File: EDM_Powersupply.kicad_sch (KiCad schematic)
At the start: 23 parts, among them J1 Screw_Terminal_01x02, Q1 IPW65R037C6, U1 L7805, U2 STGAP2SM, U3 RP2040, U4 MGJ2D051505SC, U5 LMV331

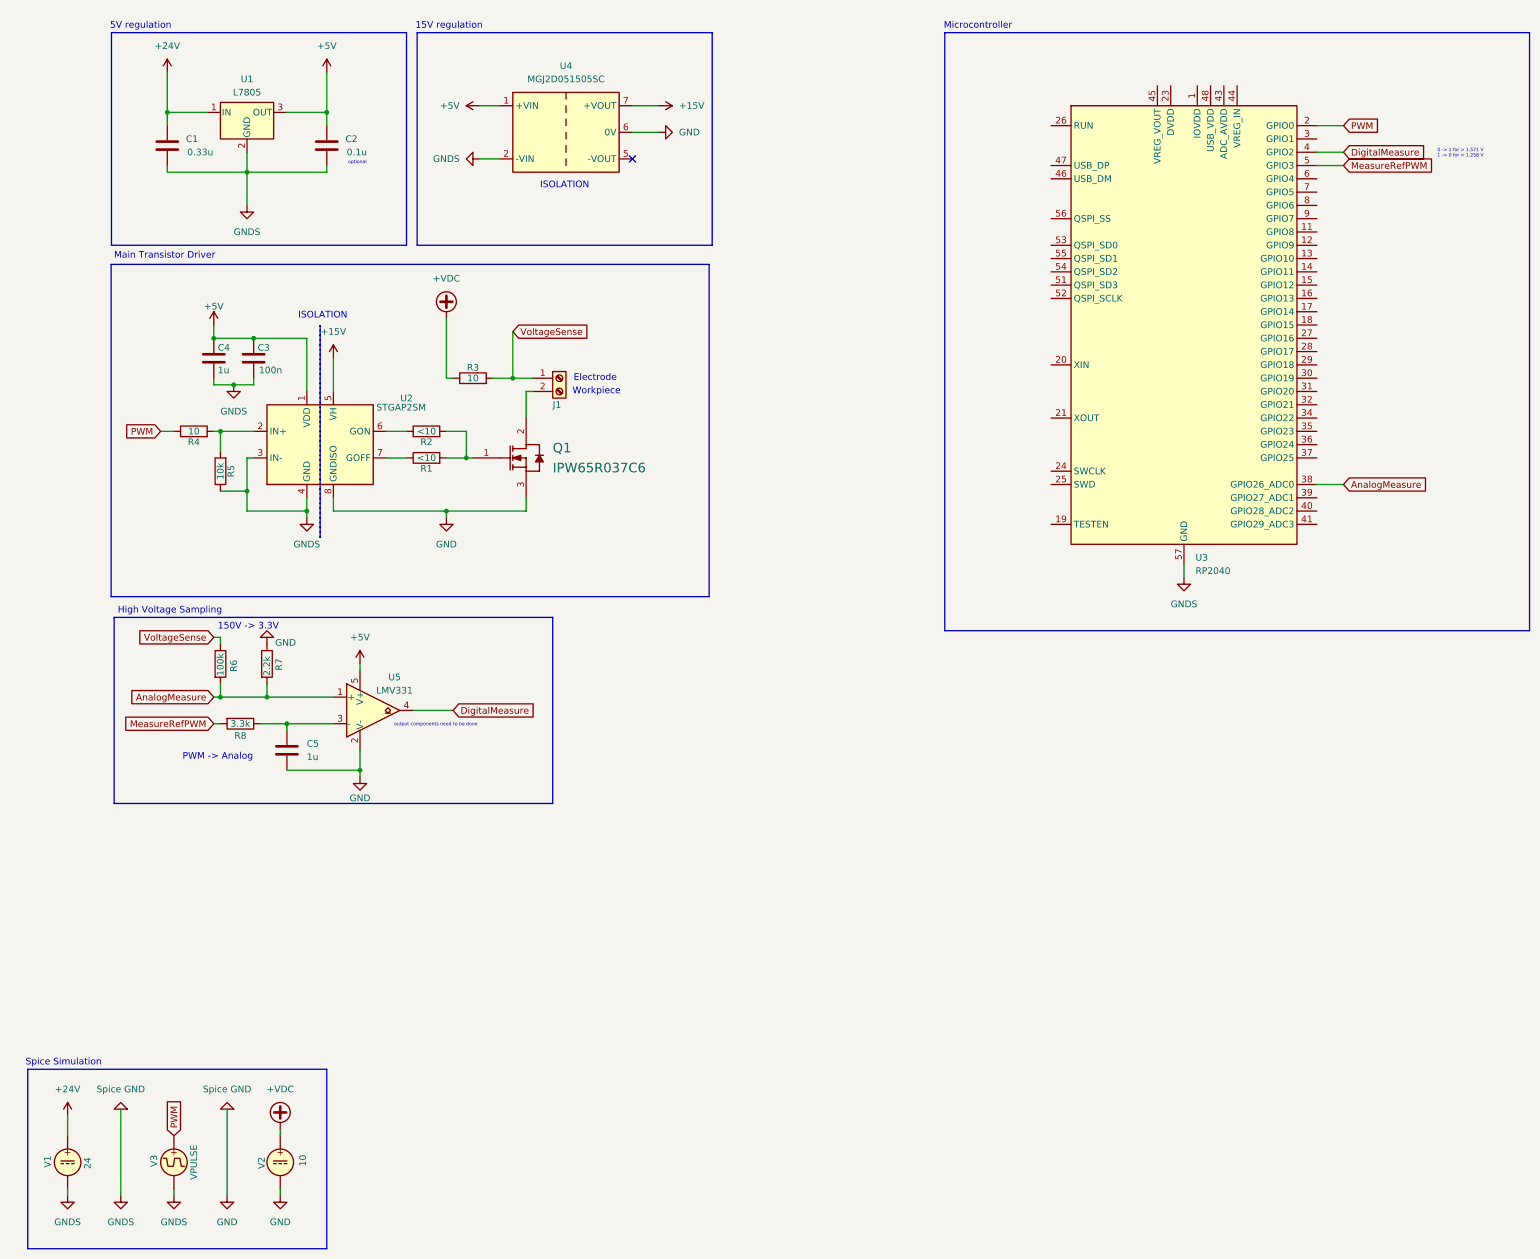
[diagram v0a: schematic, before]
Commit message: Full Reordering and added test pads
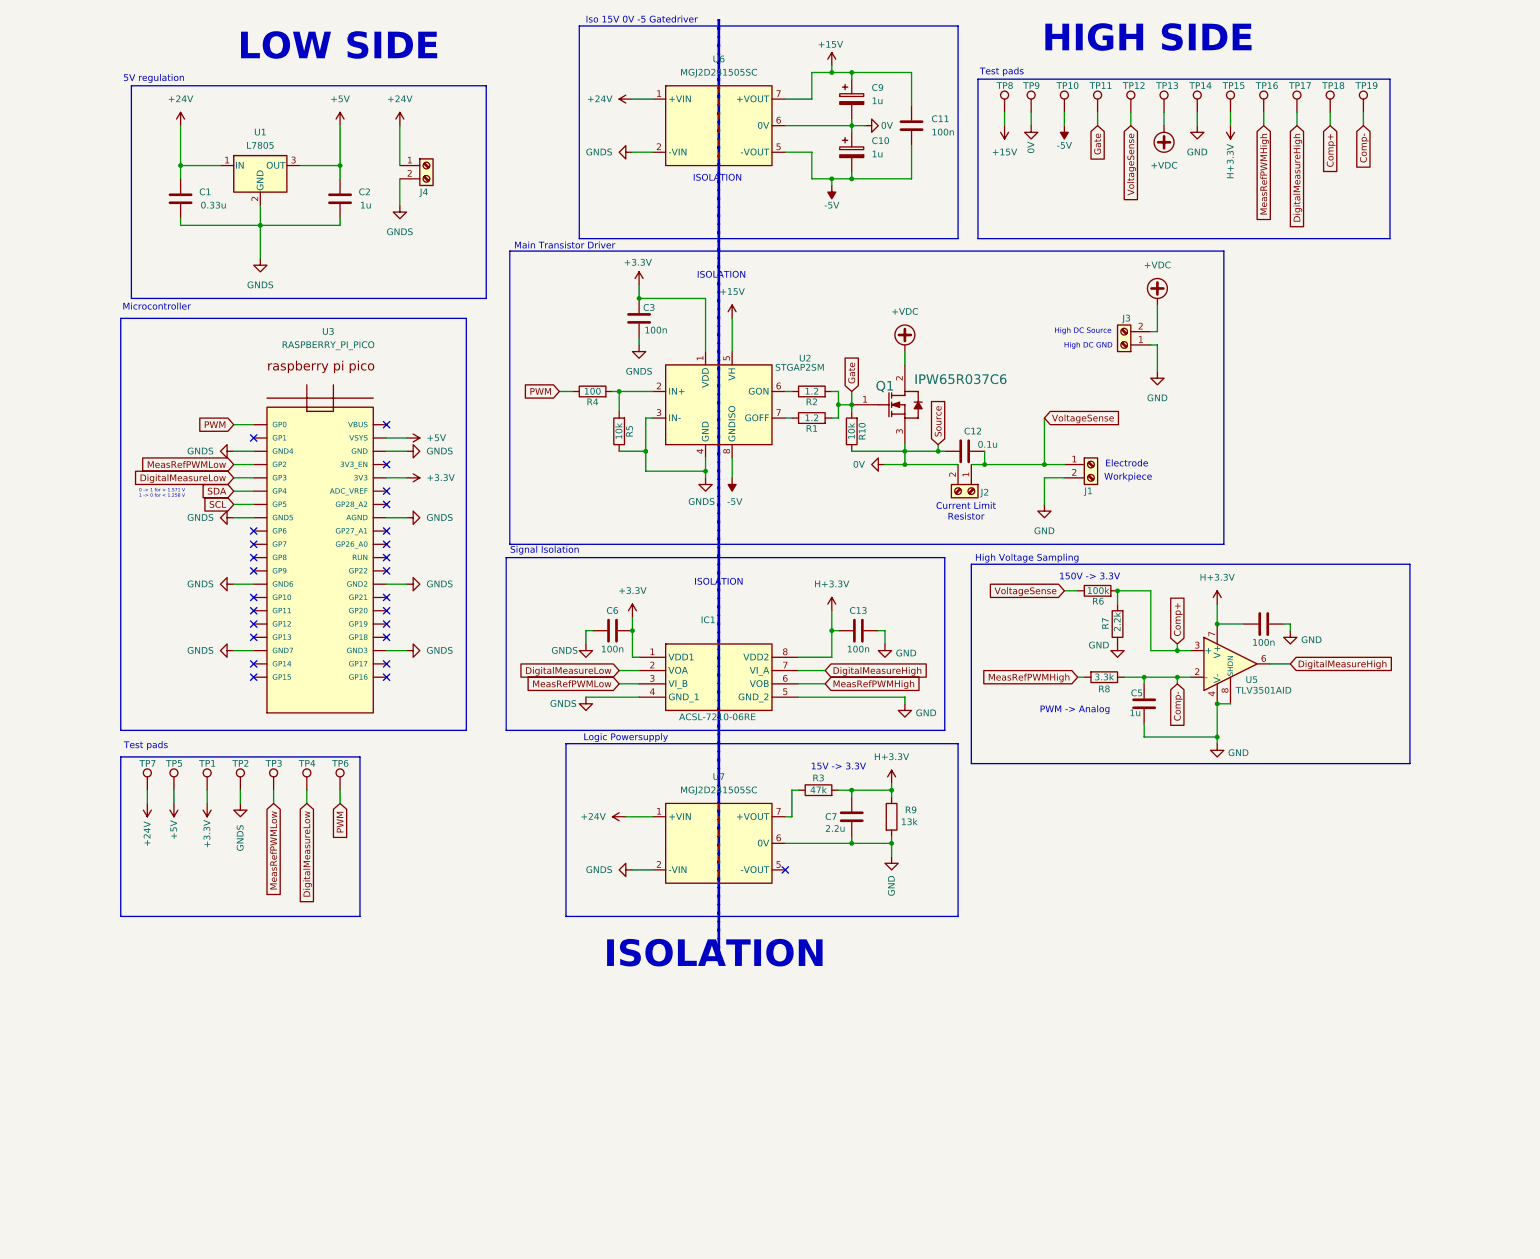
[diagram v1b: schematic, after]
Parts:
- removed C4: 1u, symbol Device:C
- removed U3: RP2040, Package_DFN_QFN:QFN-56-1EP_7x7mm_P0.4mm_EP3.2x3.2mm, symbol MCU_RaspberryPi:RP2040
- removed U4: MGJ2D051505SC, Converter_DCDC:Converter_DCDC_Murata_MGJ2DxxxxxxSC_THT, symbol Converter_DCDC:MGJ2D051505SC
- removed U5: LMV331, symbol Comparator:LMV331
- removed V1: 24, symbol Simulation_SPICE:VDC
- removed V2: 10, symbol Simulation_SPICE:VDC
- removed V3: VPULSE, symbol Simulation_SPICE:VPULSE
- added C10, C9: 1u, symbol Device:C_Polarized
- added C11, C13, C6, C8: 100n, symbol Device:C
- added C12: 0.1u, symbol Device:C
- added C7: 2.2u, symbol Device:C
- added IC1: ACSL-7210-06RE, SOIC127P600X175-8N, symbol ACSL-7210-06RE:ACSL-7210-06RE
- added J2, J3, J4: Screw_Terminal_01x02, symbol Connector:Screw_Terminal_01x02
- added R10: 10k, symbol Device:R
- added R9: 13k, symbol Device:R
- added TP1, TP10: Low Side 3.3V, symbol Connector:TestPoint
- added TP11, TP2: Signal GND, symbol Connector:TestPoint
- added TP12, TP3: PWM Reference, symbol Connector:TestPoint
- added TP13, TP4: Digital Meas Low Side, symbol Connector:TestPoint
- added TP14, TP15, TP16, TP17, TP18, TP19, TP6: PWM Signal Gen, symbol Connector:TestPoint
- added TP5, TP9: Low Side 5V, symbol Connector:TestPoint
- added TP7, TP8: Low Side 24V, symbol Connector:TestPoint
- added U3: RASPBERRY_PI_PICO, RASPBERRY_PI_PICO:RASPBERRY_PI_PICO, symbol RASPBERRY_PI_PICO:RASPBERRY_PI_PICO
- added U5: TLV3501AID, Package_SO:SOIC-8_3.9x4.9mm_P1.27mm, symbol Comparator:TLV3501AID
- added U6, U7: MGJ2D241505SC, Converter_DCDC:Converter_DCDC_Murata_MGJ2DxxxxxxSC_THT, symbol Converter_DCDC:MGJ2D241505SC
- C2: value 0.1u -> 1u
- R1, R2: value <10 -> 1.2
- R3: value 10 -> 47k
- R4: value 10 -> 100
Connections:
- net +15V: now also C11.1, C9.1, TP8.1, U6.7 (+VOUT)
- net +24V: now also J4.1 (Pin_1), TP7.1, U6.1 (+VIN), U7.1 (+VIN)
- net +5V: now also TP5.1, U3.VSYS; no longer C3.1, U2.1 (VDD)
- net +VDC: now also Q1.2 (DRAIN), J3.2 (Pin_2), TP13.1; no longer R3.1
- net GND: now also J1.2 (Pin_2), C13.2, C7.2, C8.2, IC1.5 (GND_2), J3.1 (Pin_1), R9.2, TP14.1, U5.4 (V-), U5.8 (SHDN), U7.6 (0V); no longer C1.2, C2.2, C3.2, Q1.3 (SOURCE), R5.1, U1.2 (GND), U2.3 (IN-), U2.4 (GND), U2.8 (GNDISO)
- net PWM: now also TP6.1, U3.GP0
- net VoltageSense: now also C12.2, J2.1 (Pin_1), TP12.1; no longer R3.2
- net Gate: now reaches Q1.1 (GATE), R1.2, R2.2
- net Gate: now also R10.2, TP11.1
- net Comp-: now reaches C5.1, R8.1
- net Comp-: now also TP19.1, U5.2 (-)
- net AnalogMeasure renamed Comp+
- net Comp+: now also TP18.1, U5.3 (+)
- net MeasureRefPWM renamed MeasRefPWMHigh
- net MeasRefPWMHigh: now also IC1.6 (VOB), TP16.1
- new net: R3.1, U7.7 (+VOUT)
- new net +3.3V: C3.1, C6.2, IC1.1 (VDD1), TP1.1, U2.1 (VDD), U3.3V3
- new net -5V: C10.2, C11.2, TP10.1, U2.8 (GNDISO), U6.5 (-VOUT)
- new net 0V: C10.1, C12.1, C9.2, J2.2 (Pin_2), Q1.3 (SOURCE), R10.1, TP9.1, U6.6 (0V)
- new net DigitalMeasureHigh: IC1.7 (VI_A), TP17.1, U5.6
- new net DigitalMeasureLow: IC1.2 (VOA), TP4.1, U3.GP3
- new net GNDS: C1.2, C2.2, C3.2, C6.1, IC1.4 (GND_1), J4.2 (Pin_2), R5.1, TP2.1, U1.2 (GND), U2.3 (IN-), U2.4 (GND), U3.AGND, U3.GND, U3.GND2, U3.GND3, U3.GND4, U3.GND5, U3.GND6, U3.GND7, U6.2 (-VIN), U7.2 (-VIN)
- new net H+3.3V: C13.1, C7.1, C8.1, IC1.8 (VDD2), R3.2, R9.1, TP15.1, U5.7 (V+)
- new net MeasRefPWMLow: IC1.3 (VI_B), TP3.1, U3.GP2
- new net SCL: U3.GP5
- new net SDA: U3.GP4
- no-connect marks 1 -> 26
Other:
- note added: "15V -> 3.3V"
- note added: "Current Limit Resistor"
- note added: "HIGH SIDE"
- note added: "High DC GND"
- note added: "High DC Source"
- note added: "Iso 15V 0V -5 Gatedriver"
- note added: "LOW SIDE"
- note added: "Logic Powersupply"
- note added: "Signal Isolation"
- note added: "Test pads"
- note removed: "15V regulation"
- note removed: "Spice Simulation"
- note removed: "optional"
- note removed: "output components need to be done"
- title: (none) -> EDM Transistor Powersupply
- moved on the sheet: C1, C2, C3, C5, J1, Q1, R1, R2, R4, R5, R6, R7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

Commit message: Updated ERC
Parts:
- removed TP1, TP10: Low Side 3.3V, symbol Connector:TestPoint
- removed TP11, TP2: Signal GND, symbol Connector:TestPoint
- removed TP12, TP3: PWM Reference, symbol Connector:TestPoint
- removed TP13, TP4: Digital Meas Low Side, symbol Connector:TestPoint
- removed TP14, TP15, TP16, TP17, TP18, TP19, TP6: PWM Signal Gen, symbol Connector:TestPoint
- removed TP5, TP9: Low Side 5V, symbol Connector:TestPoint
- removed TP7, TP8: Low Side 24V, symbol Connector:TestPoint
- added J1: Conn_01x13_Pin, Connector_PinHeader_2.54mm:PinHeader_1x13_P2.54mm_Vertical, symbol Connector:Conn_01x13_Pin
- added J6: Conn_01x07_Pin, Connector_PinHeader_2.54mm:PinHeader_1x07_P2.54mm_Vertical, symbol Connector:Conn_01x07_Pin
- added J7: Conn_01x03_Pin, symbol Connector:Conn_01x03_Pin
- C1: renamed from C9; footprint (none) -> Capacitor_SMD:C_0805_2012Metric_Pad1.18x1.45mm_HandSolder
- C10: renamed from C13; footprint (none) -> Capacitor_SMD:C_0805_2012Metric_Pad1.18x1.45mm_HandSolder
- C11: renamed from C5; footprint (none) -> Capacitor_SMD:C_0805_2012Metric_Pad1.18x1.45mm_HandSolder
- C12: renamed from C7; footprint (none) -> Capacitor_SMD:C_0805_2012Metric_Pad1.18x1.45mm_HandSolder
- C2: renamed from C11; footprint (none) -> Capacitor_SMD:C_0805_2012Metric_Pad1.18x1.45mm_HandSolder
- C3: renamed from C10; footprint (none) -> Capacitor_SMD:C_0805_2012Metric_Pad1.18x1.45mm_HandSolder
- C4: renamed from C1; footprint (none) -> Capacitor_SMD:C_0805_2012Metric_Pad1.18x1.45mm_HandSolder
- C5: renamed from C2; footprint (none) -> Capacitor_SMD:C_0805_2012Metric_Pad1.18x1.45mm_HandSolder
- C6: renamed from C3; footprint (none) -> Capacitor_SMD:C_0805_2012Metric_Pad1.18x1.45mm_HandSolder
- C7: renamed from C12; footprint (none) -> Capacitor_SMD:C_0805_2012Metric_Pad1.18x1.45mm_HandSolder
- C8: value 100n -> 0.1u; footprint (none) -> Capacitor_SMD:C_0805_2012Metric_Pad1.18x1.45mm_HandSolder
- C9: renamed from C6; footprint (none) -> Capacitor_SMD:C_0805_2012Metric_Pad1.18x1.45mm_HandSolder
- IC1: footprint SOIC127P600X175-8N -> Connector_PinHeader_2.54mm:PinHeader_1x13_P2.54mm_Vertical
- J2: renamed from J4; footprint (none) -> TerminalBlock_4Ucon:TerminalBlock_4Ucon_1x02_P3.50mm_Vertical
- J3: footprint (none) -> TerminalBlock_4Ucon:TerminalBlock_4Ucon_1x02_P3.50mm_Vertical
- J4: renamed from J1; footprint (none) -> TerminalBlock_4Ucon:TerminalBlock_4Ucon_1x02_P3.50mm_Vertical
- J5: renamed from J2; footprint (none) -> TerminalBlock_4Ucon:TerminalBlock_4Ucon_1x02_P3.50mm_Vertical
- Q1: footprint INF-PG-TO247-3-44 -> (none)
- R1: renamed from R4; footprint (none) -> Resistor_THT:R_Axial_DIN0207_L6.3mm_D2.5mm_P7.62mm_Horizontal
- R10: renamed from R9; footprint (none) -> Resistor_THT:R_Axial_DIN0207_L6.3mm_D2.5mm_P7.62mm_Horizontal
- R2, R6, R7, R8: footprint (none) -> Resistor_THT:R_Axial_DIN0207_L6.3mm_D2.5mm_P7.62mm_Horizontal
- R3: renamed from R1; footprint (none) -> Resistor_THT:R_Axial_DIN0207_L6.3mm_D2.5mm_P7.62mm_Horizontal
- R4: renamed from R5; footprint (none) -> Resistor_THT:R_Axial_DIN0207_L6.3mm_D2.5mm_P7.62mm_Horizontal
- R5: renamed from R10; footprint (none) -> Resistor_THT:R_Axial_DIN0207_L6.3mm_D2.5mm_P7.62mm_Horizontal
- R9: renamed from R3; footprint (none) -> Resistor_THT:R_Axial_DIN0207_L6.3mm_D2.5mm_P7.62mm_Horizontal
- renumbered U6 to U1, U1 to U2, U2 to U3, U3 to U4, U7 to U6
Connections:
- net +15V: now also J1.11 (Pin_11)
- net +24V: now also J6.6 (Pin_6)
- net +3.3V: now also J6.4 (Pin_4)
- net +5V: now also J6.5 (Pin_5)
- net +VDC: now also J1.13 (Pin_13)
- net -5V: now also J1.9 (Pin_9)
- net 0V: now also J1.10 (Pin_10)
- net Comp+: now also J1.2 (Pin_2)
- net Comp-: now also J1.1 (Pin_1)
- net DigitalMeasureHigh: now also J1.3 (Pin_3)
- net DigitalMeasureLow: now also J6.2 (Pin_2)
- net GND: now also J1.12 (Pin_12)
- net GNDS: now also J6.7 (Pin_7), J7.3 (Pin_3)
- net Gate: now also J1.7 (Pin_7)
- net H+3.3V: now also J1.8 (Pin_8)
- net MeasRefPWMHigh: now also J1.4 (Pin_4)
- net MeasRefPWMLow: now also J6.3 (Pin_3)
- net PWM: now also J6.1 (Pin_1)
- net SCL: now also J7.1 (Pin_1)
- net SDA: now also J7.2 (Pin_2)
- net VoltageSense: now also J1.5 (Pin_5)
- new net Source: J1.6 (Pin_6)
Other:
- note added: "Dont populate pad 13"
- note added: "I2C interface"
- moved on the sheet: C7, C9, J5

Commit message: good
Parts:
- added HS1: Heatsink, Heatsink:Heatsink_Fischer_SK104-STCB_35x13mm__2xDrill3.5mm_ScrewM3, symbol Mechanical:Heatsink
- C1, C11, C12, C3, C5: footprint Capacitor_SMD:C_0805_2012Metric_Pad1.18x1.45mm_HandSolder -> Capacitor_THT:CP_Radial_D10.0mm_P7.50mm
- IC1: footprint Connector_PinHeader_2.54mm:PinHeader_1x13_P2.54mm_Vertical -> ACSL-7210-06RE:ACSL-7210-06RE
- J2, J3, J4, J5: footprint TerminalBlock_4Ucon:TerminalBlock_4Ucon_1x02_P3.50mm_Vertical -> TerminalBlock:TerminalBlock_Altech_AK300-2_P5.00mm
- J7: footprint (none) -> Connector_PinHeader_2.54mm:PinHeader_1x03_P2.54mm_Vertical
- Q1: footprint (none) -> IPW65R037C6:IPW65R037C6
- R1, R10, R2, R3, R4, R5, R6, R7, R8, R9: footprint Resistor_THT:R_Axial_DIN0207_L6.3mm_D2.5mm_P7.62mm_Horizontal -> Resistor_THT:R_Axial_DIN0411_L9.9mm_D3.6mm_P12.70mm_Horizontal
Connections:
- net GNDS: no longer U4.AGND
- net GON: now reaches R2.1, U3.6 (GON)
- net GOFF: now reaches R3.1, U3.7 (GOFF)
- net IN+: now reaches R1.2, R4.2, U3.2 (IN+)
- net +VOUT: now reaches R9.1, U6.7 (+VOUT)
- net Source: no longer names the net of J1.6 (Pin_6)
- no-connect marks 26 -> 28
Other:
- note added: "Optional extra probe pin"
- moved on the sheet: C7, C9, J5, Q1, R2, R3, R5

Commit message: PCB Done?
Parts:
- added H1, H2, H3, H4: MountingHole, MountingHole:MountingHole_3.2mm_M3, symbol Mechanical:MountingHole
- R1, R10, R2, R3, R4, R5, R6, R7, R8, R9: footprint Resistor_THT:R_Axial_DIN0411_L9.9mm_D3.6mm_P12.70mm_Horizontal -> Resistor_THT:R_Axial_DIN0207_L6.3mm_D2.5mm_P7.62mm_Horizontal
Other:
- note added: "Mounting Holes"

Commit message: final?
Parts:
- removed HS1: Heatsink, Heatsink:Heatsink_Fischer_SK104-STCB_35x13mm__2xDrill3.5mm_ScrewM3, symbol Mechanical:Heatsink
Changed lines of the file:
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@@
-	)
-	(symbol
-		(lib_id "Mechanical:Heatsink")
-		(at 43.18 34.29 0)
-		(unit 1)
-		(exclude_from_sim yes)
-		(in_bom yes)
-		(on_board yes)
-		(dnp no)
-		(fields_autoplaced yes)
-		(property "Reference" "HS1"
-			(at 46.99 31.1149 0)
-			(effects
-				(font
-					(size 1.27 1.27)
-				)
-				(justify left)
-			)
-		)
-		(property "Value" "Heatsink"
-			(at 46.99 33.6549 0)
-			(effects
-				(font
-					(size 1.27 1.27)
-				)
-				(justify left)
-			)
-		)
-		(property "Footprint" "Heatsink:Heatsink_Fischer_SK104-STCB_35x13mm__2xDrill3.5mm_ScrewM3"
-			(at 43.4848 34.29 0)
-			(effects
-				(font
-					(size 1.27 1.27)
-				)
-				(hide yes)
-			)
-		)
-		(property "Datasheet" "~"
-			(at 43.4848 34.29 0)
-			(effects
-				(font
-					(size 1.27 1.27)
-				)
-				(hide yes)
-			)
-		)
-		(property "Description" "Heatsink"
-			(at 43.18 34.29 0)
-			(effects
-				(font
-					(size 1.27 1.27)
-				)
-				(hide yes)
-			)
-		)
-		(instances
-			(project "EDM_Powersupply"
-				(path "/25514edd-baec-405d-b564-4fa05365ce84"
-					(reference "HS1")
-					(unit 1)
-				)
-			)
-		)
 	)
 	(symbol
